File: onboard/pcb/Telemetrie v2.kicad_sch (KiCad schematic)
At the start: 78 parts, among them J1 Conn_02x03_Odd_Even, J2 Conn_01x02_Pin, J3 SMA SMD, J4 Conn_01x04_Pin, J5 Conn_01x02_Pin, M1 Conn_01x01_Pin, M2 Conn_01x01_Pin, M3 Conn_01x01_Pin, M4 Conn_01x01_Pin, U1 AVR128DB64x-xPT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

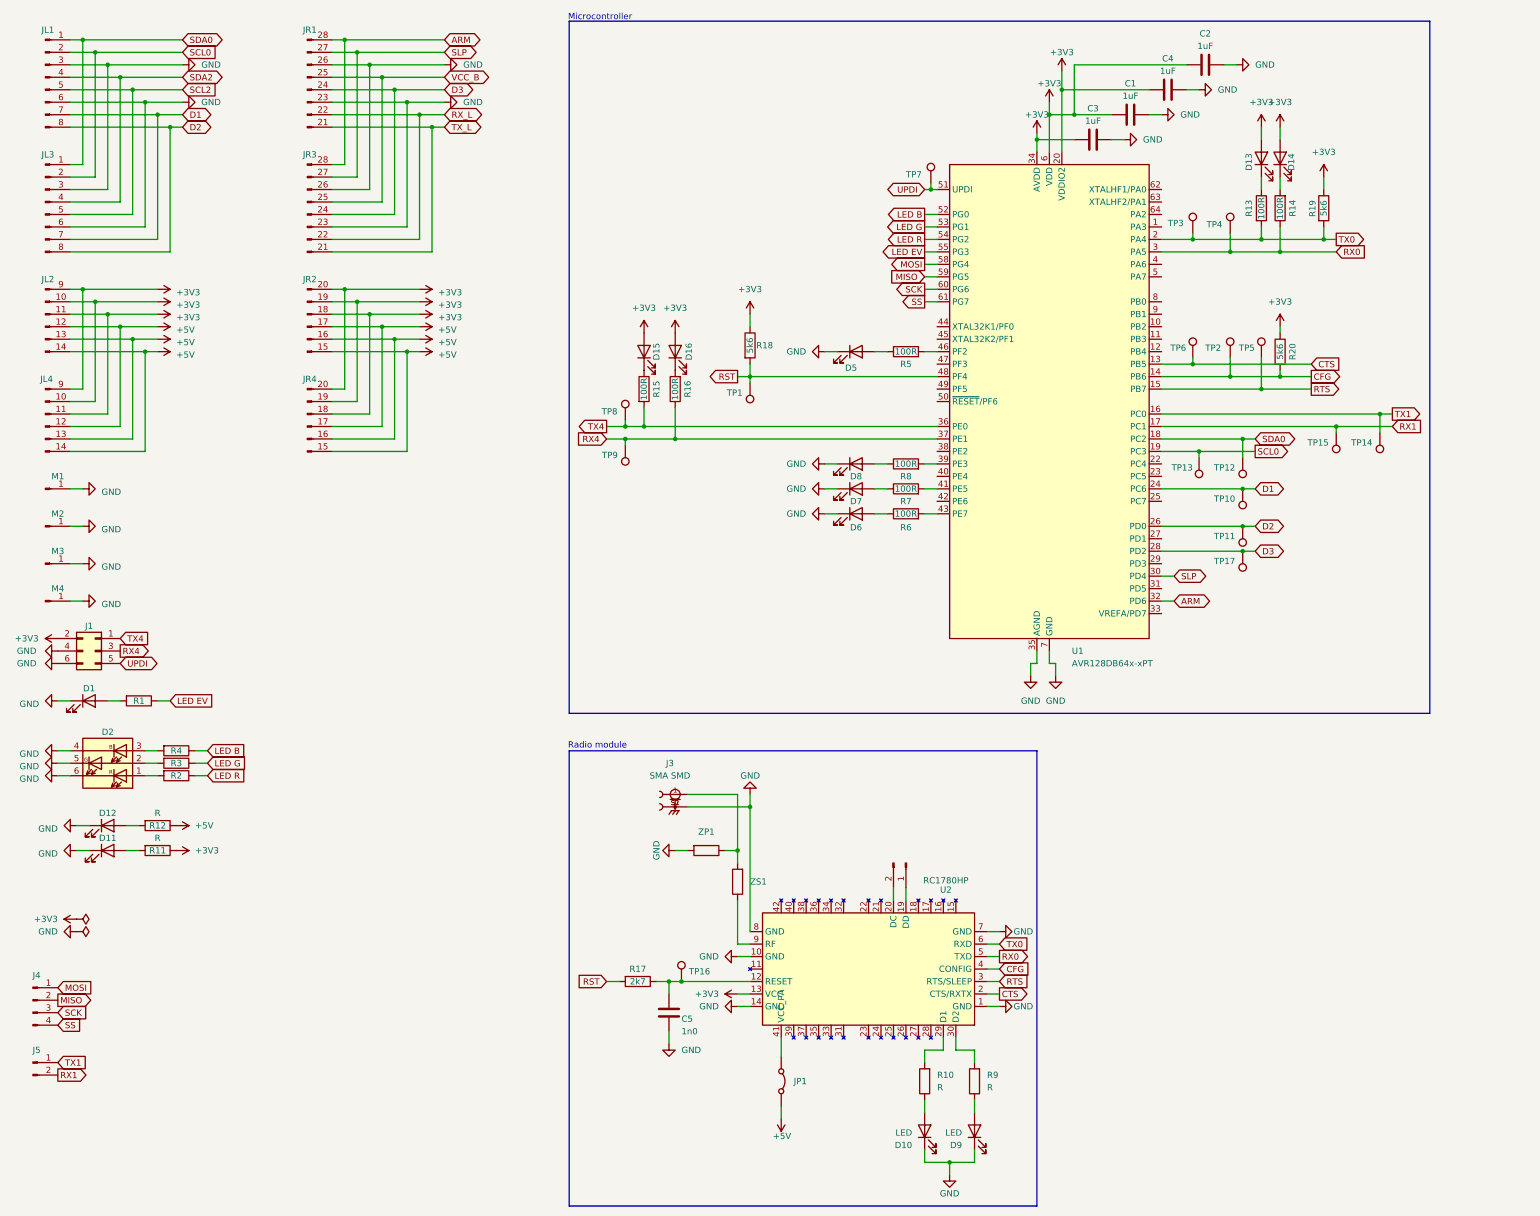
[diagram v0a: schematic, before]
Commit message: adjusted schematic and pcb according to the design rule check
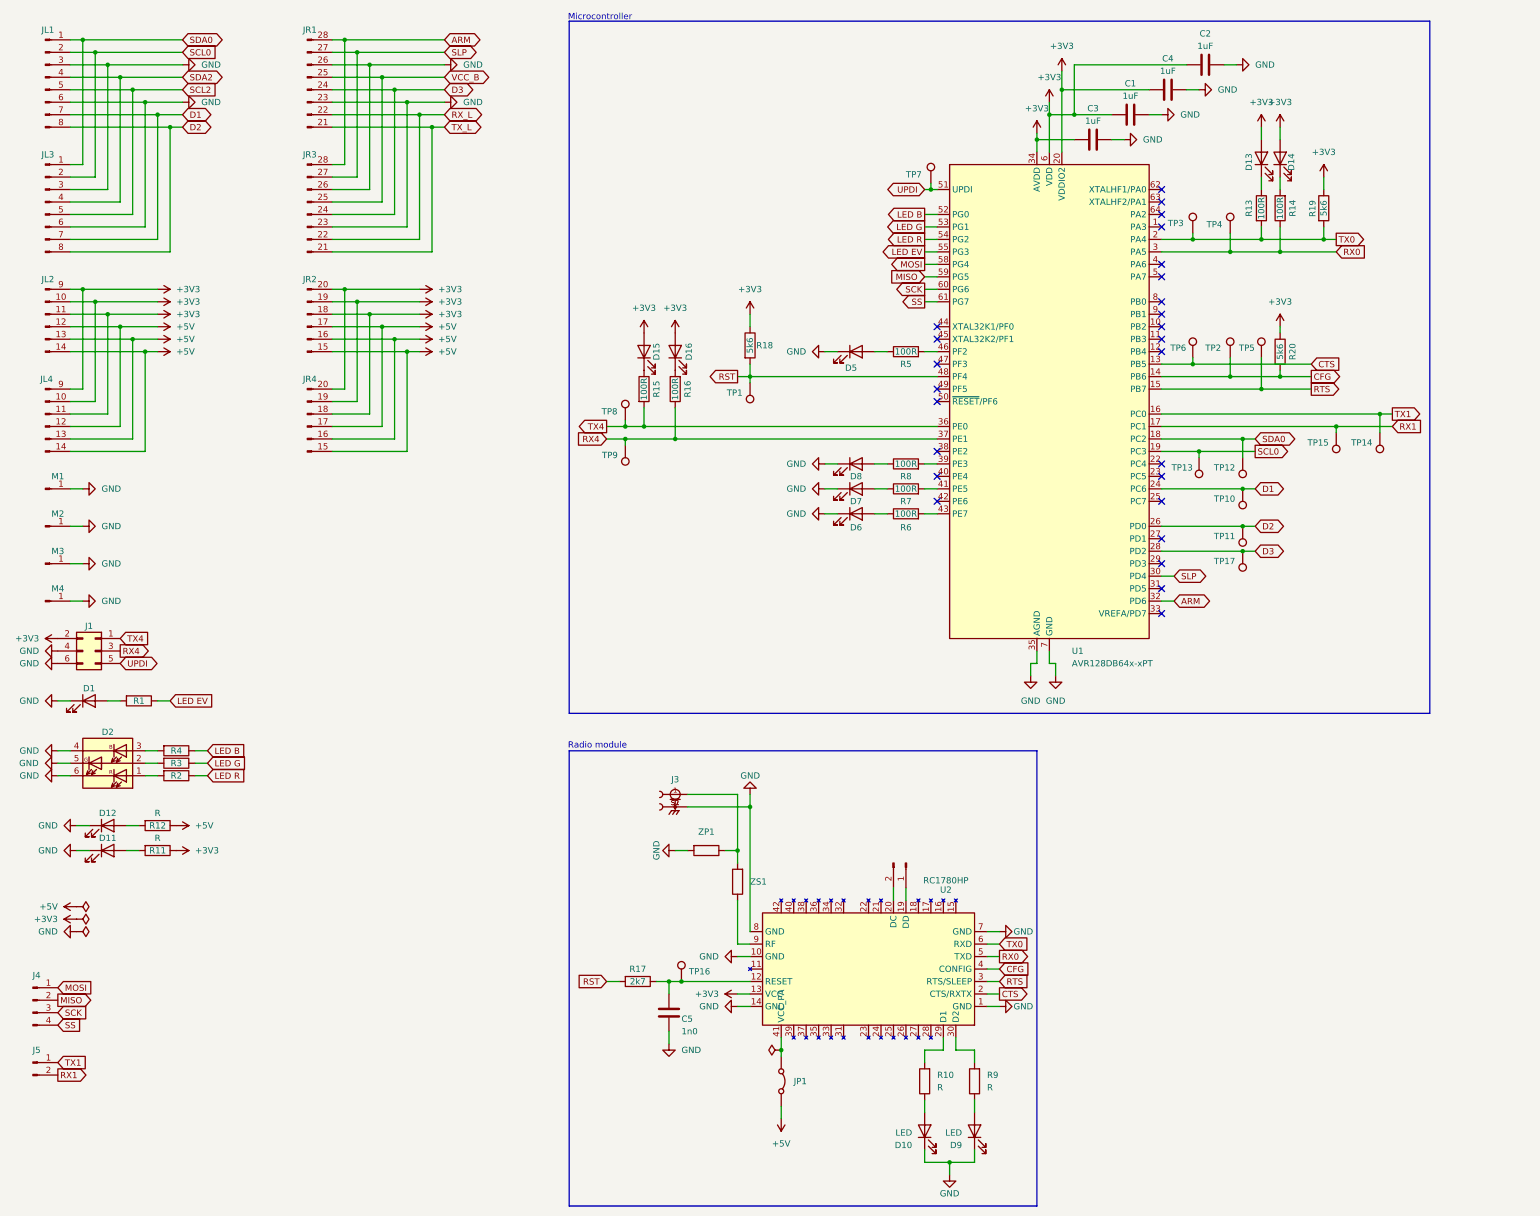
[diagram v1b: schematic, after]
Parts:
- J3: symbol New_Library:CONSMA001-SMD-G-T -> Library:CONSMA001-SMD-G-T
- U2: symbol New_Library:RC1780 -> Library:RC1780
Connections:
- no-connect marks 0 -> 26

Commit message: prep for production version
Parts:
- added LS1: CMT-0525-75-SMT-TR, Footprints:XDCR_CMT-0525-75-SMT-TR, symbol Library:CMT-0525-75-SMT-TR
- added R21: 5k6, Resistor_SMD:R_0805_2012Metric_Pad1.20x1.40mm_HandSolder, symbol Device:R
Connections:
- net ARM: now also R21.1
- net GND: now also LS1.N, R21.2
- net at U1.12 (PB4): now also LS1.P
- no-connect marks 26 -> 25

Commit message: updated custom libraries and silkscreen
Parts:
- J3: footprint Footprints:SMA_connector_smd -> Footprints:SMA Connector CONSMA001-SMD-G-T; symbol Library:CONSMA001-SMD-G-T -> Library:SMA Connector CONSMA001-SMD-G-T
- JP1: footprint Footprints:Jumper -> Footprints:Solder Jumper
- LS1: footprint Footprints:XDCR_CMT-0525-75-SMT-TR -> Footprints:Buzzer XDCR_CMT-0525-75-SMT-TR; symbol Library:CMT-0525-75-SMT-TR -> Library:Buzzer CMT-0525-75-SMT-TR
- M1, M2, M3, M4: footprint Footprints:m4hole -> Footprints:M4 Mounting Hole
- TP1, TP10, TP11, TP12, TP13, TP14, TP15, TP16, TP17, TP2, TP3, TP4, TP5, TP6, TP7, TP8, TP9: footprint Footprints:TestPoint -> Footprints:Test Point
- U2: footprint Footprints:RC1780HP -> Footprints:Radiocrafts RC1780HP-RC232; symbol Library:RC1780 -> Library:Radiocrafts RC1780HP-RC232
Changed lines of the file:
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@@
 			)
 		)
-		(property "Footprint" "Footprints:m4hole"
+		(property "Footprint" "Footprints:M4 Mounting Hole"
 			(at 26.67 115.57 0)
 			(effects
@@
 			)
 		)
-		(property "Footprint" "Footprints:TestPoint"
+		(property "Footprint" "Footprints:Test Point"
 			(at 265.43 109.22 0)
 			(effects
@@
 			)
 		)
-		(property "Footprint" "Footprints:TestPoint"
+		(property "Footprint" "Footprints:Test Point"
 			(at 161.29 215.9 0)
 			(effects
@@
 			)
 		)
-		(property "Footprint" "Footprints:TestPoint"
+		(property "Footprint" "Footprints:Test Point"
 			(at 279.4 88.9 0)
 			(effects
@@
 			)
 		)
-		(property "Footprint" "Footprints:TestPoint"
+		(property "Footprint" "Footprints:Test Point"
 			(at 139.7 106.68 0)
 			(effects
@@
 			)
 		)
-		(property "Footprint" "Footprints:TestPoint"
+		(property "Footprint" "Footprints:Test Point"
 			(at 265.43 63.5 0)
 			(effects
@@
 			)
 		)
-		(property "Footprint" "Footprints:TestPoint"
+		(property "Footprint" "Footprints:Test Point"
 			(at 273.05 63.5 0)
 			(effects
@@
 	)
 	(symbol
-		(lib_id "Library:CONSMA001-SMD-G-T")
+		(lib_id "Library:SMA Connector CONSMA001-SMD-G-T")
 		(at 154.94 177.8 0)
 		(unit 1)
@@
 			)
 		)
-		(property "Footprint" "Footprints:SMA_connector_smd"
+		(property "Footprint" "Footprints:SMA Connector CONSMA001-SMD-G-T"
 			(at 154.94 177.8 0)
 			(effects
@@
 			)
 		)
-		(property "Footprint" "Footprints:Jumper"
+		(property "Footprint" "Footprints:Solder Jumper"
 			(at 176.53 236.22 0)
 			(effects
@@
 			)
 		)
-		(property "Footprint" "Footprints:TestPoint"
+		(property "Footprint" "Footprints:Test Point"
 			(at 212.09 53.34 0)
 			(effects
@@
 			)
 		)
-		(property "Footprint" "Footprints:m4hole"
+		(property "Footprint" "Footprints:M4 Mounting Hole"
 			(at 26.67 138.43 0)
 			(effects
@@
 			)
 		)
-		(property "Footprint" "Footprints:TestPoint"
+		(property "Footprint" "Footprints:Test Point"
 			(at 256.54 109.22 0)
 			(effects
@@
 			)
 		)
-		(property "Footprint" "Footprints:TestPoint"
+		(property "Footprint" "Footprints:Test Point"
 			(at 293.37 104.14 0)
 			(effects
@@
 			)
 		)
-		(property "Footprint" "Footprints:TestPoint"
+		(property "Footprint" "Footprints:Test Point"
 			(at 284.48 104.14 0)
 			(effects
@@
 			)
 		)
-		(property "Footprint" "Footprints:TestPoint"
+		(property "Footprint" "Footprints:Test Point"
 			(at 273.05 88.9 0)
 			(effects
@@
 	)
 	(symbol
-		(lib_id "Library:CMT-0525-75-SMT-TR")
+		(lib_id "Library:Buzzer CMT-0525-75-SMT-TR")
 		(at 298.45 80.01 0)
 		(unit 1)
@@
 				)
 				(justify left)
+				(hide yes)
 			)
 		)
-		(property "Footprint" "Footprints:XDCR_CMT-0525-75-SMT-TR"
+		(property "Footprint" "Footprints:Buzzer XDCR_CMT-0525-75-SMT-TR"
 			(at 298.45 80.01 0)
 			(effects
@@
 			)
 		)
-		(property "Footprint" "Footprints:TestPoint"
+		(property "Footprint" "Footprints:Test Point"
 			(at 265.43 128.27 0)
 			(effects
@@
 	)
 	(symbol
-		(lib_id "Library:RC1780")
+		(lib_id "Library:Radiocrafts RC1780HP-RC232")
 		(at 218.44 227.33 180)
 		(unit 1)
@@
 			)
 		)
-		(property "Footprint" "Footprints:RC1780HP"
+		(property "Footprint" "Footprints:Radiocrafts RC1780HP-RC232"
 			(at 218.44 227.33 0)
 			(effects
@@
 			)
 		)
-		(property "Footprint" "Footprints:m4hole"
+		(property "Footprint" "Footprints:M4 Mounting Hole"
 			(at 26.67 130.81 0)
 			(effects
@@
 			)
 		)
-		(property "Footprint" "Footprints:TestPoint"
+		(property "Footprint" "Footprints:Test Point"
 			(at 265.43 115.57 0)
 			(effects
@@
 			)
 		)
-		(property "Footprint" "Footprints:TestPoint"
+		(property "Footprint" "Footprints:Test Point"
 			(at 149.86 101.6 0)
 			(effects
@@
 			)
 		)
-		(property "Footprint" "Footprints:m4hole"
+		(property "Footprint" "Footprints:M4 Mounting Hole"
 			(at 26.67 123.19 0)
 			(effects
@@
 			)
 		)
-		(property "Footprint" "Footprints:TestPoint"
+		(property "Footprint" "Footprints:Test Point"
 			(at 265.43 123.19 0)
 			(effects
@@
 			)
 		)
-		(property "Footprint" "Footprints:TestPoint"
+		(property "Footprint" "Footprints:Test Point"
 			(at 165.1 93.98 0)
 			(effects
@@
 			)
 		)
-		(property "Footprint" "Footprints:TestPoint"
+		(property "Footprint" "Footprints:Test Point"
 			(at 265.43 88.9 0)
 			(effects
